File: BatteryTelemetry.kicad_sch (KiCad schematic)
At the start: 137 parts, among them IC1 BQ76925PWR, IC2 BQ76925PWR, IC3 BQ76925PWR, IC4 BQ76925PWR, J1 Conn_01x07_Pin, J2 Conn_01x07_Pin, J3 Conn_01x07_Pin, J4 Conn_01x07_Pin, J5 USB_C_Receptacle_USB2.0, J6 Conn_01x04_Socket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

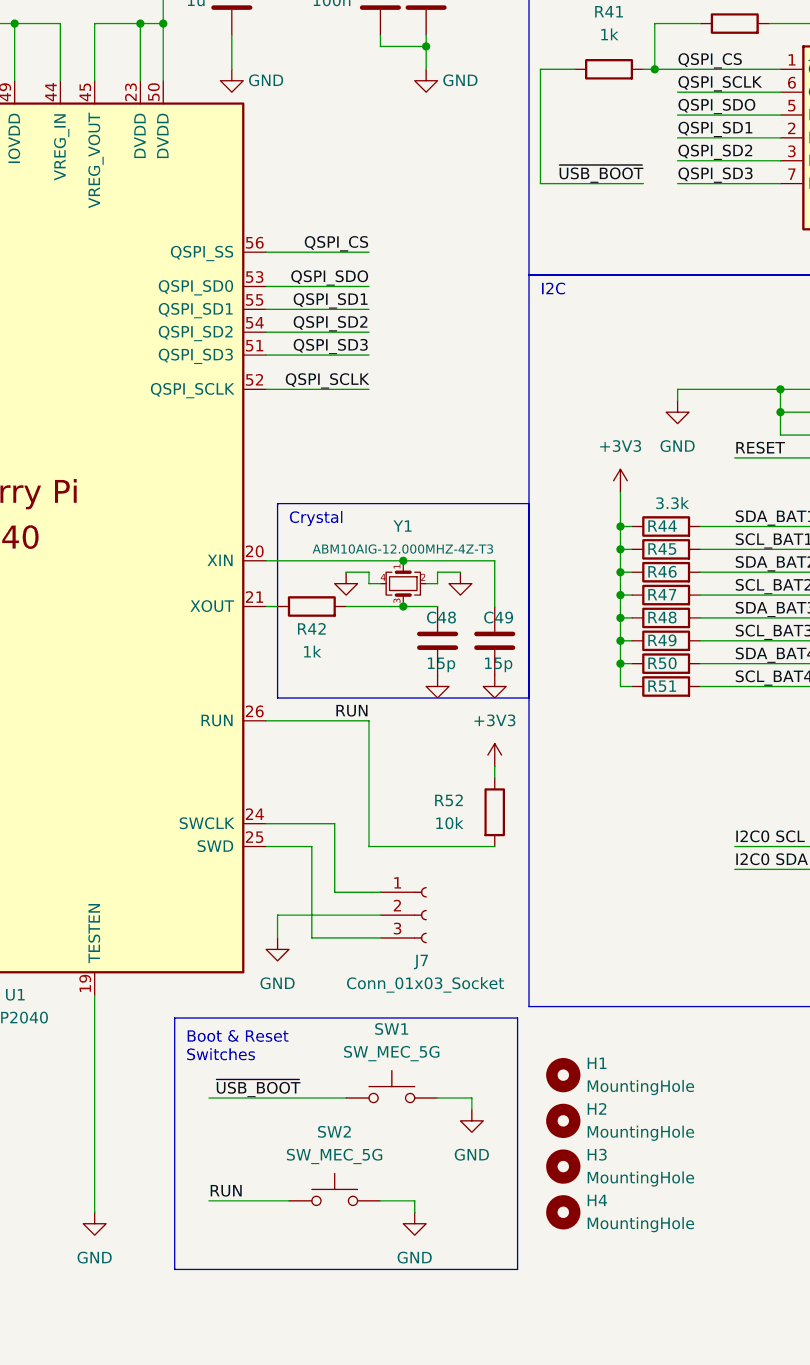
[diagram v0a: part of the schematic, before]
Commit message: button fixed
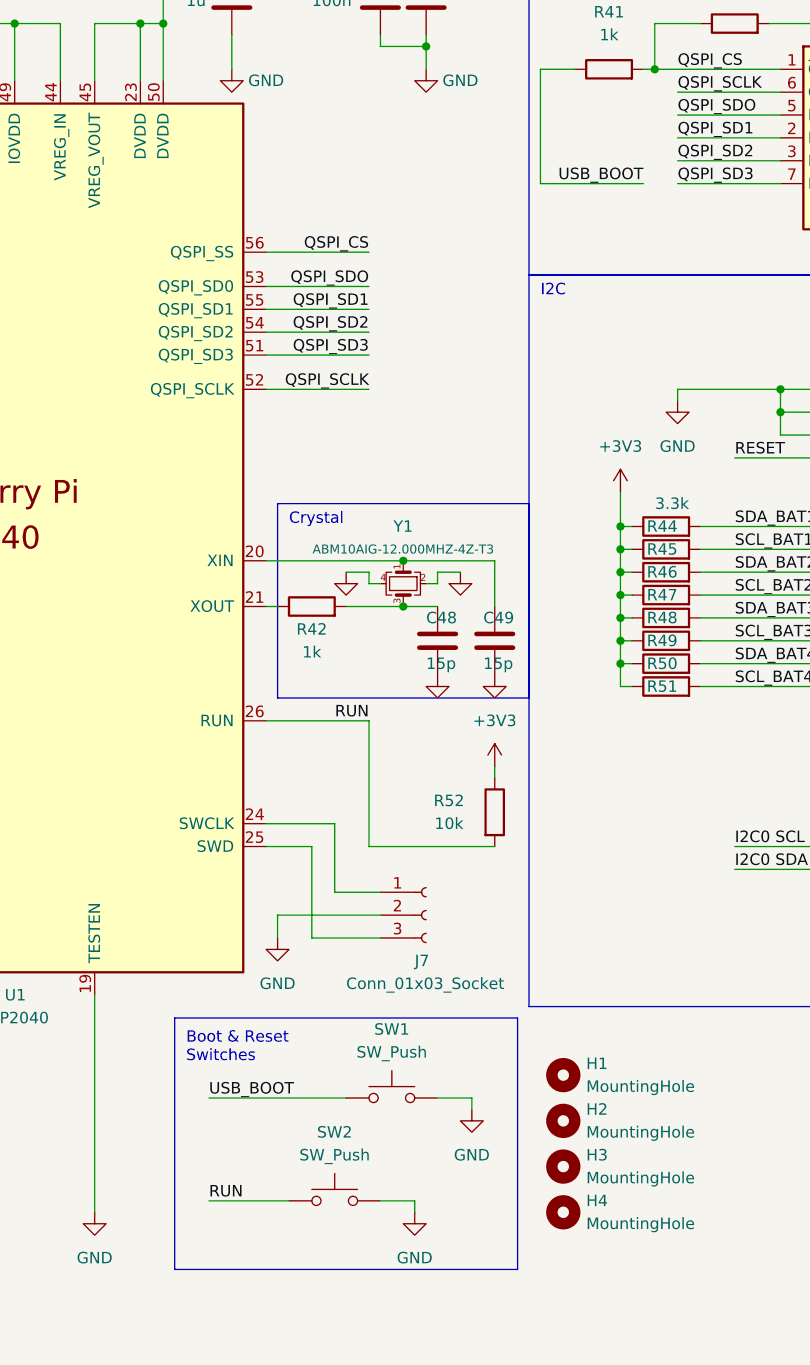
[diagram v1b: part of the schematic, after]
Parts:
- removed SW1, SW2: SW_MEC_5G, Button_Switch_THT:SW_PUSH_6mm_H4.3mm, symbol Switch:SW_MEC_5G
- added SW1, SW2: SW_Push, Button_Switch_THT:SW_PUSH_1P1T_6x3.5mm_H4.3_APEM_MJTP1243, symbol Switch:SW_Push
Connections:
- net GND: now also SW1.2, SW2.2
- net RUN: now also SW2.1
- net ~{USB_BOOT} renamed USB_BOOT
- net USB_BOOT: now also SW1.1

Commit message: Layout Complete
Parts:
- C37: footprint Capacitor_SMD:C_0805_2012Metric -> Capacitor_SMD:C_0805_2012Metric_Pad1.18x1.45mm_HandSolder
- H1, H2, H3, H4: footprint MountingHole:MountingHole_3.2mm_M3 -> MountingHole:MountingHole_3.2mm_M3_DIN965_Pad
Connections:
- net SCL_BAT1: now also U4.5 (SC0); no longer U4.7 (SC1)
- net SCL_BAT2: now also U4.7 (SC1); no longer U4.9 (SC2)
- net SCL_BAT3: now also U4.9 (SC2); no longer U4.11 (SC3)
- net SCL_BAT4: now also U4.11 (SC3); no longer U4.14 (SC4)
- net SDA_BAT1: now also U4.4 (SD0); no longer U4.6 (SD1)
- net SDA_BAT2: now also U4.6 (SD1); no longer U4.8 (SD2)
- net SDA_BAT3: now also U4.8 (SD2); no longer U4.10 (SD3)
- net SDA_BAT4: now also U4.10 (SD3); no longer U4.13 (SD4)
- no-connect marks 59 -> 57

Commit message: Updated Layout
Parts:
- added TP1, TP10, TP11, TP12, TP13, TP14, TP15, TP2, TP3, TP4, TP5, TP6, TP7, TP8, TP9: TestPoint, TestPoint:TestPoint_THTPad_D1.5mm_Drill0.7mm, symbol Connector:TestPoint
- H1, H2, H3, H4: symbol Mechanical:MountingHole -> Mechanical:MountingHole_Pad; now left out of the parts list
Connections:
- net +3V3: now also TP3.1
- net BAT1: now also TP11.1
- net BAT3: now also TP12.1
- net I2C0 SCL: now also TP15.1
- net I2C0 SDA: now also TP14.1
- net RESET: now also TP13.1
- net SCL_BAT1: now also TP8.1
- net SCL_BAT3: now also TP10.1
- net SDA_BAT1: now also TP7.1
- net SDA_BAT3: now also TP9.1
- net V3_BAT: now also SW3.4, TP1.1
- net V3_EXT: now also SW3.6, TP4.1
- net V3_USB: now also TP5.1
- net at C34.1, D4.1 (K), D5.1 (K)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: now also TP6.1
- net at D6.2 (A), SW3.2 (B): now also SW3.5, TP2.1
- new net Chassis: H1.1, H2.1, H3.1, H4.1
- no-connect marks 57 -> 59
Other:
- title: Battery Telemetry -> Battery Telemetry Schematic 
- moved on the sheet: R34, R35, R36, R44, R45, R46, R47, R48, R49, R50, R51

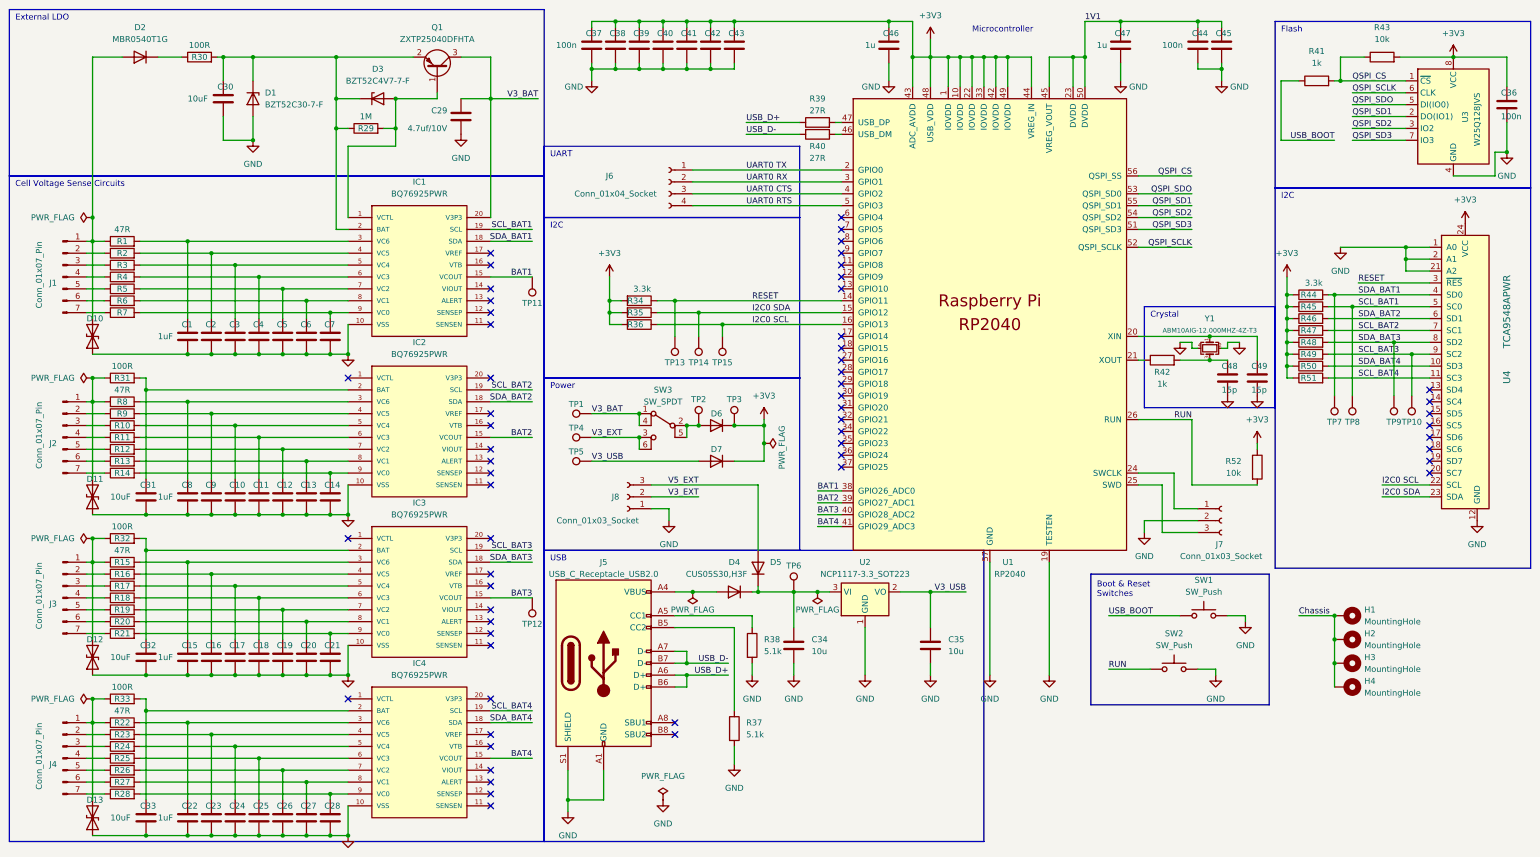
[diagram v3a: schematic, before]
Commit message: RC circuit for VCout
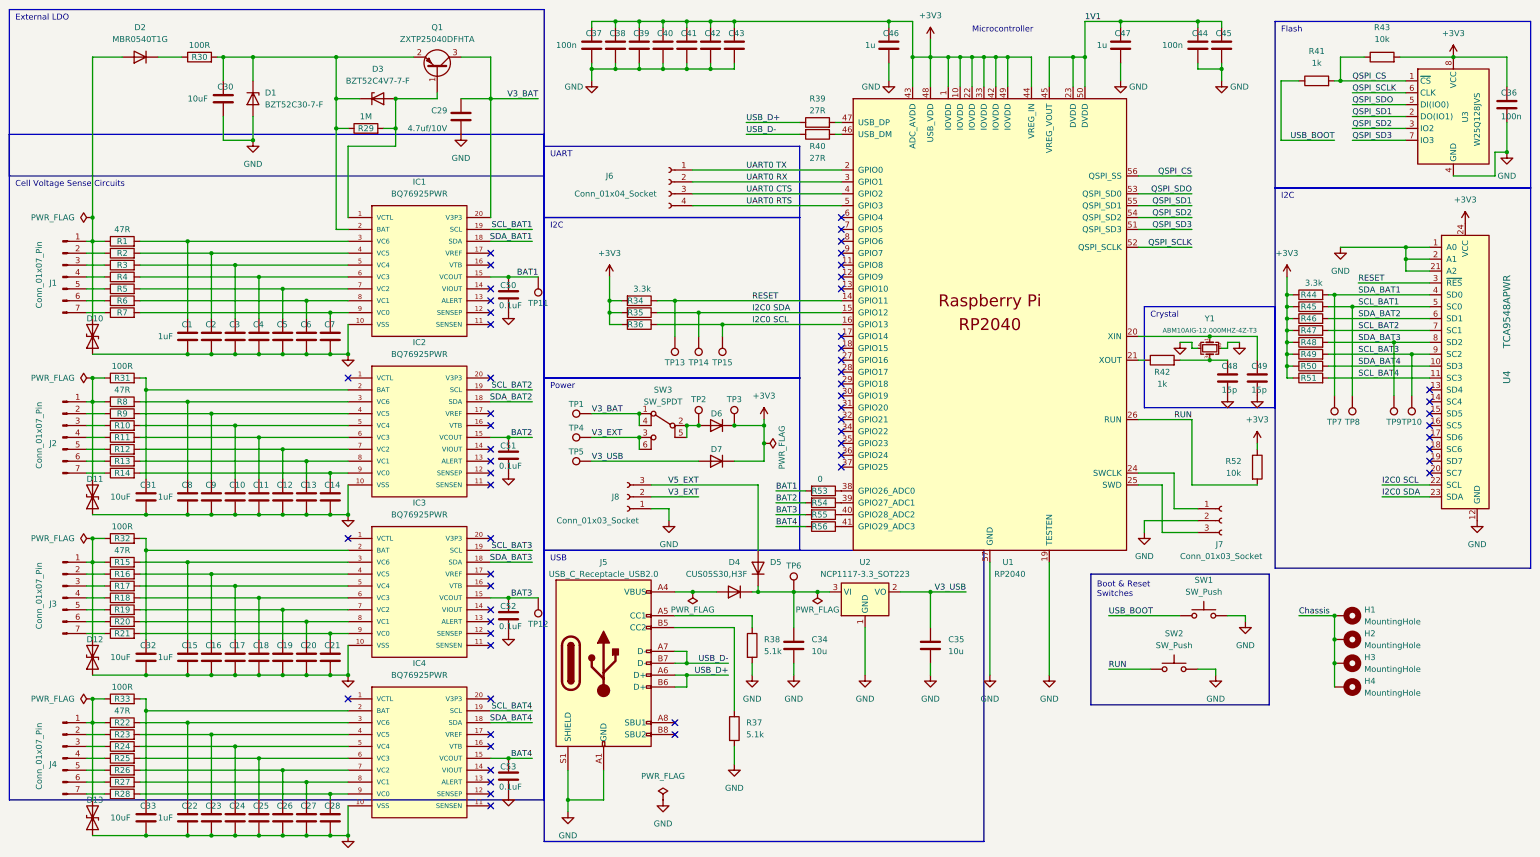
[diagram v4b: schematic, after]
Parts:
- added C50, C51, C52, C53: 0.1uF, Capacitor_SMD:C_0805_2012Metric_Pad1.18x1.45mm_HandSolder, symbol Device:C
- added R53, R54, R55, R56: 0, Resistor_SMD:R_0805_2012Metric_Pad1.20x1.40mm_HandSolder, symbol Device:R
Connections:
- net BAT1: now also C50.1, R53.2; no longer U1.38 (GPIO26_ADC0)
- net BAT2: now also C51.1, R54.2; no longer U1.39 (GPIO27_ADC1)
- net BAT3: now also C52.1, R55.2; no longer U1.40 (GPIO28_ADC2)
- net BAT4: now also C53.1, R56.2; no longer U1.41 (GPIO29_ADC3)
- net GND: now also C50.2, C51.2, C52.2, C53.2
- new net: R55.1, U1.40 (GPIO28_ADC2)
- new net: R56.1, U1.41 (GPIO29_ADC3)
- new net: R53.1, U1.38 (GPIO26_ADC0)
- new net: R54.1, U1.39 (GPIO27_ADC1)
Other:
- moved on the sheet: TP11, TP12

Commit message: Layout updated
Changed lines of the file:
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@@
 	)
 	(rectangle
-		(start 13.97 41.91)
-		(end 128.27 184.15)
+		(start 13.97 50.8)
+		(end 128.27 193.04)
 		(stroke
 			(width 0)
